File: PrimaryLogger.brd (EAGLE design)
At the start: 160 x 100 mm, 48 parts, among them J1 CONN_42.54_SCREW, J2 CONN_42.54_SCREW, J3 CONN_42.54_SCREW, J4 CONN_42.54_SCREW, J5 CONN_32.54_SCREW, U1 MIC2005, U2 MIC2091, U25 SN74AUP3G34DCU, U3 TPL5010DDC, U4 TXS0102DCU, U5 SN74LVC1G3157DRL, U6 TCS3400, U7 SHTC3DFN

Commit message: Continued layout progress
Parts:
- C1, C2: value (none) -> 6pF
- moved MS1 145.0 mm to (52.1, 88.9), turned to 180 degrees
- moved R8 140.8 mm to (24.1, 19.1)
- moved R7 139.8 mm to (26.7, 63.5)
- moved C11 137.6 mm to (29.2, 30.5), turned to 180 degrees
- moved J7 134.2 mm to (17.8, 14.0), turned to 180 degrees
- moved J6 133.4 mm to (24.1, 14.0)
- moved R6 133.1 mm to (21.6, 63.5), turned to 90 degrees
- moved U7 133.1 mm to (29.2, 27.9), turned to 90 degrees
- moved J5 132.6 mm to (31.8, 14.0), turned to 180 degrees
- moved U5 132.1 mm to (24.1, 63.5)
- moved J8 129.5 mm to (8.89, 14.0), turned to 180 degrees
- moved C10 126.7 mm to (29.2, 20.3)
- moved U6 124.1 mm to (29.2, 22.9), turned to 90 degrees
- moved U25 94.8 mm to (33.0, 77.5), turned to 90 degrees
- moved SD1 84.8 mm to (51.3, 83.3), turned to 90 degrees
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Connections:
- new net GPIOXA: J5.2, MS1.8
- new net N$10: MS1.10
- new net N$9: MS1.9
- net 3V3_EXT: now also J5.1
- net GND: now also J5.3
- net GPIO1A: now also MS1.5
- net GPIO2A: now also MS1.6
- net GPIO3A: now also MS1.7
- net MISO: now also MS1.13
- net MOSI: now also MS1.12
- net SCK: now also MS1.11

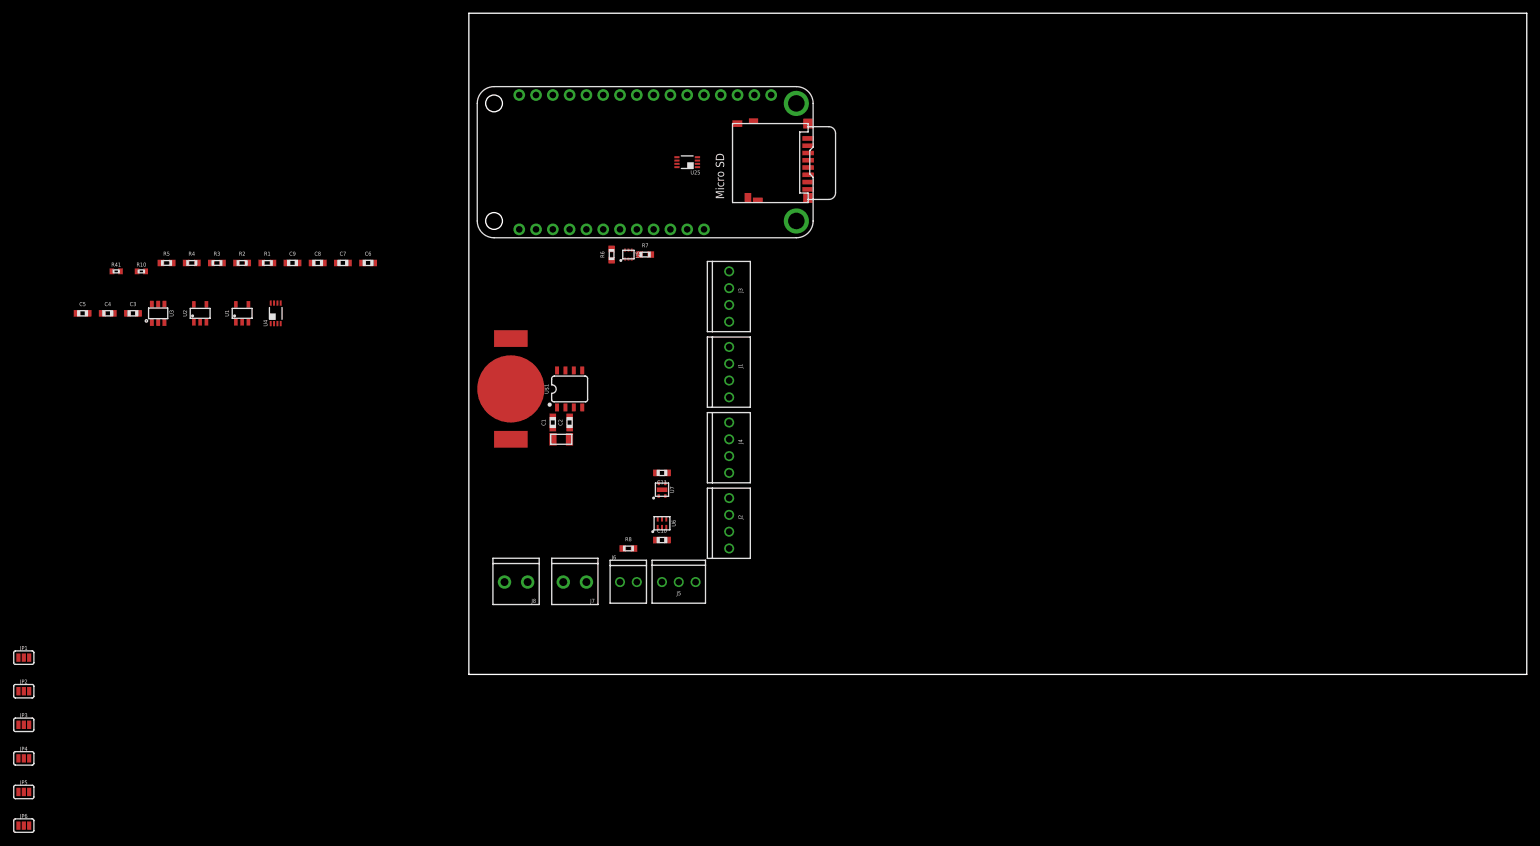
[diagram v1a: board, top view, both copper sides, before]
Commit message: Continued layout and preliminary board capture
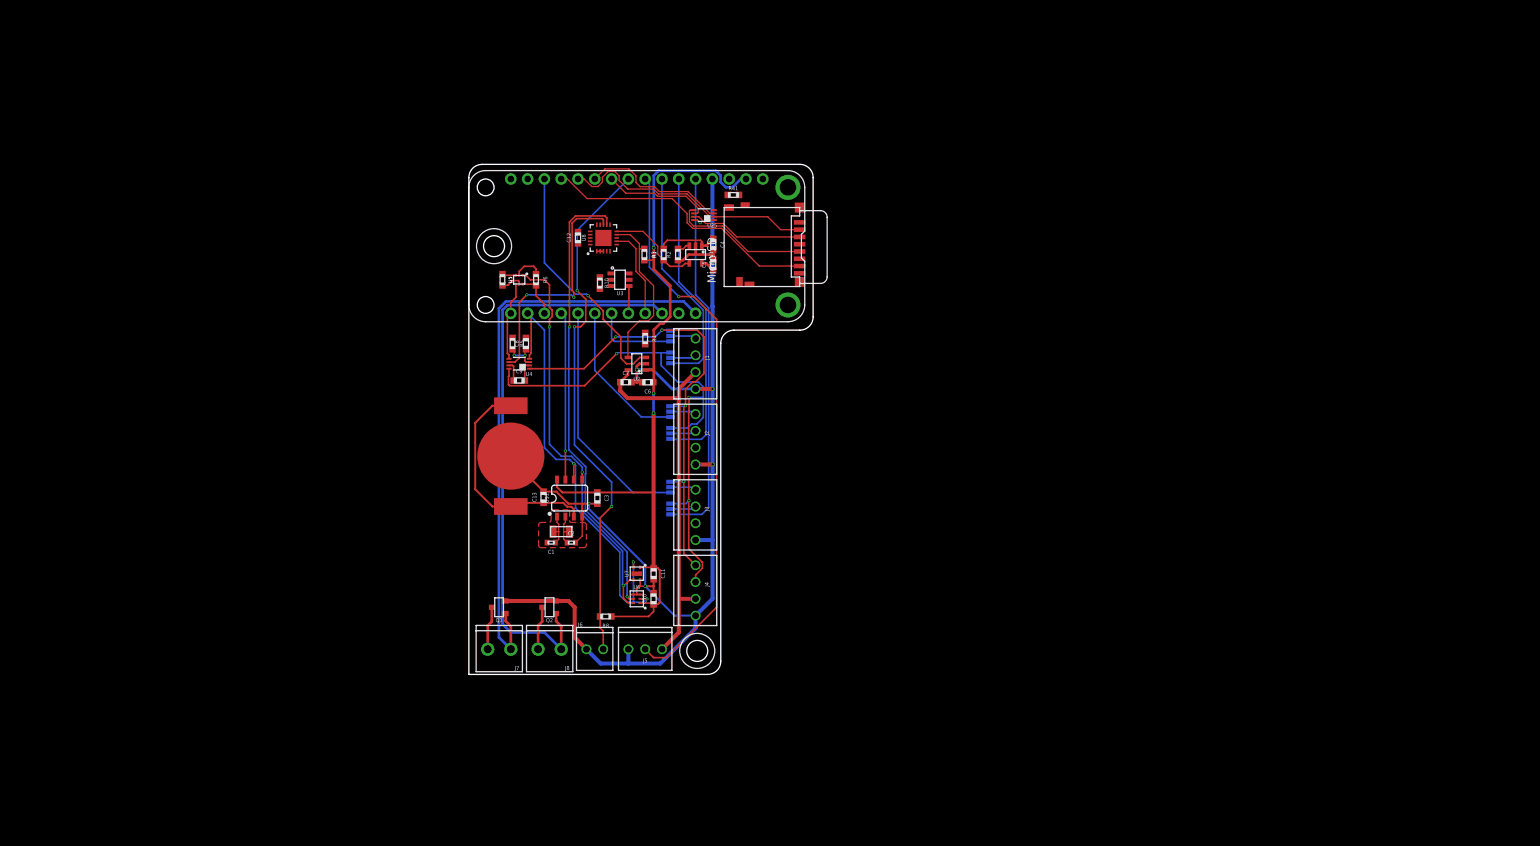
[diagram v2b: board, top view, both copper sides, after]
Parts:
- added C12: 0.1uF, bschulz_passives:C0603
- added C13: (no value), bschulz_passives:C0603
- added H1, H2: (no value), bschulz:4_40
- added Q1, Q2: DMG3404, bschulz:SOT23-3
- added U8: MCP23008QFN, bschulz:QFN20
- C1, C2: device bschulz_passives:C0603 -> bschulz_passives:C0402
- R10: device bschulz_passives:R0402 -> bschulz_passives:R0603
- R41: value 10k -> 100k; device bschulz_passives:R0402 -> bschulz_passives:R0603
- U$1: device bschulz:SO08 -> bschulz:SO08@1
- moved JP2 110.0 mm to (30.5, 47.9), flipped to the bottom, turned to 90 degrees
- moved JP4 109.4 mm to (30.5, 36.4), flipped to the bottom, turned to 90 degrees
- moved JP1 109.2 mm to (30.5, 51.2), flipped to the bottom, turned to 90 degrees
- moved JP6 108.9 mm to (30.5, 25.0), flipped to the bottom, turned to 90 degrees
- moved JP3 108.7 mm to (30.5, 39.8), flipped to the bottom, turned to 90 degrees
- moved JP5 108.1 mm to (30.5, 28.3), flipped to the bottom, turned to 90 degrees
- moved C5 95.7 mm to (37.0, 62.0), turned to 90 degrees
- moved R41 94.1 mm to (40.0, 72.5)
- moved C4 92.2 mm to (37.0, 65.0), turned to 270 degrees
- moved C3 75.6 mm to (19.4, 26.7), turned to 270 degrees
- moved U3 70.0 mm to (22.9, 59.7), turned to 270 degrees
- moved R4 69.5 mm to (26.7, 50.8), turned to 270 degrees
- moved R10 69.4 mm to (19.8, 59.2), turned to 270 degrees
- moved U1 69.2 mm to (34.3, 63.5), turned to 180 degrees
- moved U2 66.5 mm to (25.4, 47.0), turned to 90 degrees
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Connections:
- removed net N$10: MS1.10
- removed net N$9: MS1.9
- removed net VBAT+: J7.1
- removed net VSYS+: J8.1
- new net IO_EXP_INT: MS1.25, U8.7
- net 3V3: now also C12.1, R5.2, U8.18
- net 3V3_EXT_EN: now also MS1.14
- net 3V3_EXT_FAULT: now also U8.9
- net 3V3_SD_EN: now also MS1.15
- net 3V3_SD_FAULT: now also U8.10
- net GND: now also C12.2, C13.2, Q1.2, Q2.2, U8.1, U8.17, U8.2, U8.3, U8.EP; no longer R5.1
- net GPIO1A: now also MS1.7; no longer MS1.5
- net GPIO1D: now also MS1.23
- net GPIO2D: now also MS1.22
- net GPIO3A: now also MS1.5; no longer MS1.7
- net GPIO3D: now also MS1.21
- net I2C_EXT_EN: now also R5.1, U8.13; no longer R5.2
- net PAR_INT: now also U8.12
- net RST: now also U8.4
- net RTC_INT: now also MS1.20
- net SCL: now also U8.19
- net SDA_CTRL: now also MS1.19
- net SDA_OB: now also U8.20
- net SD_CD: now also U8.11
- net SD_CS: now also MS1.10
- net TIP: now also MS1.9
- net VBAT: now also C13.1
- net VBAT-: now also Q1.3
- net VBAT_FEATHER: now also J7.1, Q1.1
- net VBUS_FEATHER: now also J8.1, Q2.1
- net VSYS-: now also Q2.3
- net WD_HOLD: now also MS1.24
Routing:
- net GND: track 0.00 -> 204.7 mm, vias 0 -> 5
- net 3V3: track 0.00 -> 134.1 mm, vias 0 -> 5
- net VBAT_FEATHER: track 0.00 -> 88.9 mm
- net VBUS_FEATHER: track 0.00 -> 88.6 mm
- net GPIOXA: track 0.00 -> 85.1 mm, vias 0 -> 1
- net SDA_EXT: track 0.00 -> 83.5 mm, vias 0 -> 3
- net TIP: track 0.00 -> 79.3 mm, vias 0 -> 3
- net SCL: track 0.00 -> 71.8 mm, vias 0 -> 3
- net SCL_EXT: track 0.00 -> 71.7 mm, vias 0 -> 4
- net PAR_INT: track 0.00 -> 68.6 mm, vias 0 -> 2
- net SDA_OB: track 0.00 -> 62.6 mm, vias 0 -> 3
- net 3V3_EXT: track 0.00 -> 62.4 mm
- net GPIO3A: track 0.00 -> 56.7 mm
- net GPIO2A: track 0.00 -> 46.1 mm
- net MISO: track 0.00 -> 42.3 mm
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- added copper zone on layer 1, net GND
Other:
- board size 160 x 100 mm -> 52.1 x 77.1 mm

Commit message: BETA preliminary layout
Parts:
- removed U$1: MCP7940SOIC, bschulz:SO08@1
- added U9: MCP7940SOIC, bschulz:SO08
- moved H1 2.36 mm to (4.39, 67.1)
- moved R41 1.66 mm to (38.4, 72.4), turned to 180 degrees
- moved R4 1.55 mm to (25.4, 49.9), turned to 0 degrees
- moved C8 1.02 mm to (9.53, 49.5), turned to 0 degrees
- moved R5 1.02 mm to (5.71, 49.5), turned to 0 degrees
- moved R3 0.76 mm to (27.3, 63.5)
- moved C12 0.25 mm to (16.5, 66.3)
- turned R1 to 270 degrees
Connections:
- net 3V3: now also U9.8; no longer U$1.8
- net 3V3_EXT_EN: now also MS1.25; no longer MS1.14
- net GND: now also SD1.GND@3, SD1.GND@5, U9.4; no longer U$1.4
- net I2C_EXT_EN: now also U8.12; no longer U8.13
- net IO_EXP_INT: now also MS1.14; no longer MS1.25
- net N$1: now also U9.1; no longer U$1.1
- net N$2: now also U9.2; no longer U$1.2
- net PAR_INT: now also U8.13; no longer U8.12
- net RTC_INT: now also U9.7; no longer U$1.7
- net SCL: now also U9.6; no longer U$1.6
- net SDA_OB: now also U9.5; no longer U$1.5
- net VBAT: now also U9.3; no longer U$1.3
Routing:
- net GND: track 204.7 -> 326.0 mm, vias 5 -> 12
- net 3V3: track 134.1 -> 179.0 mm, vias 5 -> 7
- net RST: track 0.01 -> 41.7 mm, vias 0 -> 1
- net 3V3_SD: track 3.27 -> 33.6 mm, vias 1 -> 3
- net 3V3_EXT_EN: track 37.5 -> 7.16 mm, vias 1 -> 0
- net 3V3_SD_EN: track 1.92 -> 30.8 mm
- net 3V3_EXT: track 62.4 -> 86.5 mm, vias 0 -> 2
- net SD_CD: track 0.00 -> 22.3 mm, vias 0 -> 2
- net SCL: track 71.8 -> 92.3 mm, vias 3 -> 5
- net SDA_OB: track 62.6 -> 74.9 mm, vias 3 -> 5
- net 3V3_EXT_FAULT: track 25.4 -> 32.6 mm, vias 0 -> 2
- net IO_EXP_INT: track 13.7 -> 19.1 mm, vias 0 -> 2
- net I2C_EXT_EN: track 36.2 -> 39.8 mm, vias 2 -> 0
- net GPIO3A: track 56.7 -> 60.1 mm
- net N$3: track 0.00 -> 1.87 mm
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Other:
- board text added: "(1 3/16 in)"
- board text added: "(2.5 in)"
- board text added: "J10"
- board text added: "J9"
